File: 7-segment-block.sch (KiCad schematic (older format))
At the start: 23 parts, among them J1 DATA_OUT, J2 DATA_IN, U1 TPIC6C596PWR, U2 74LS125

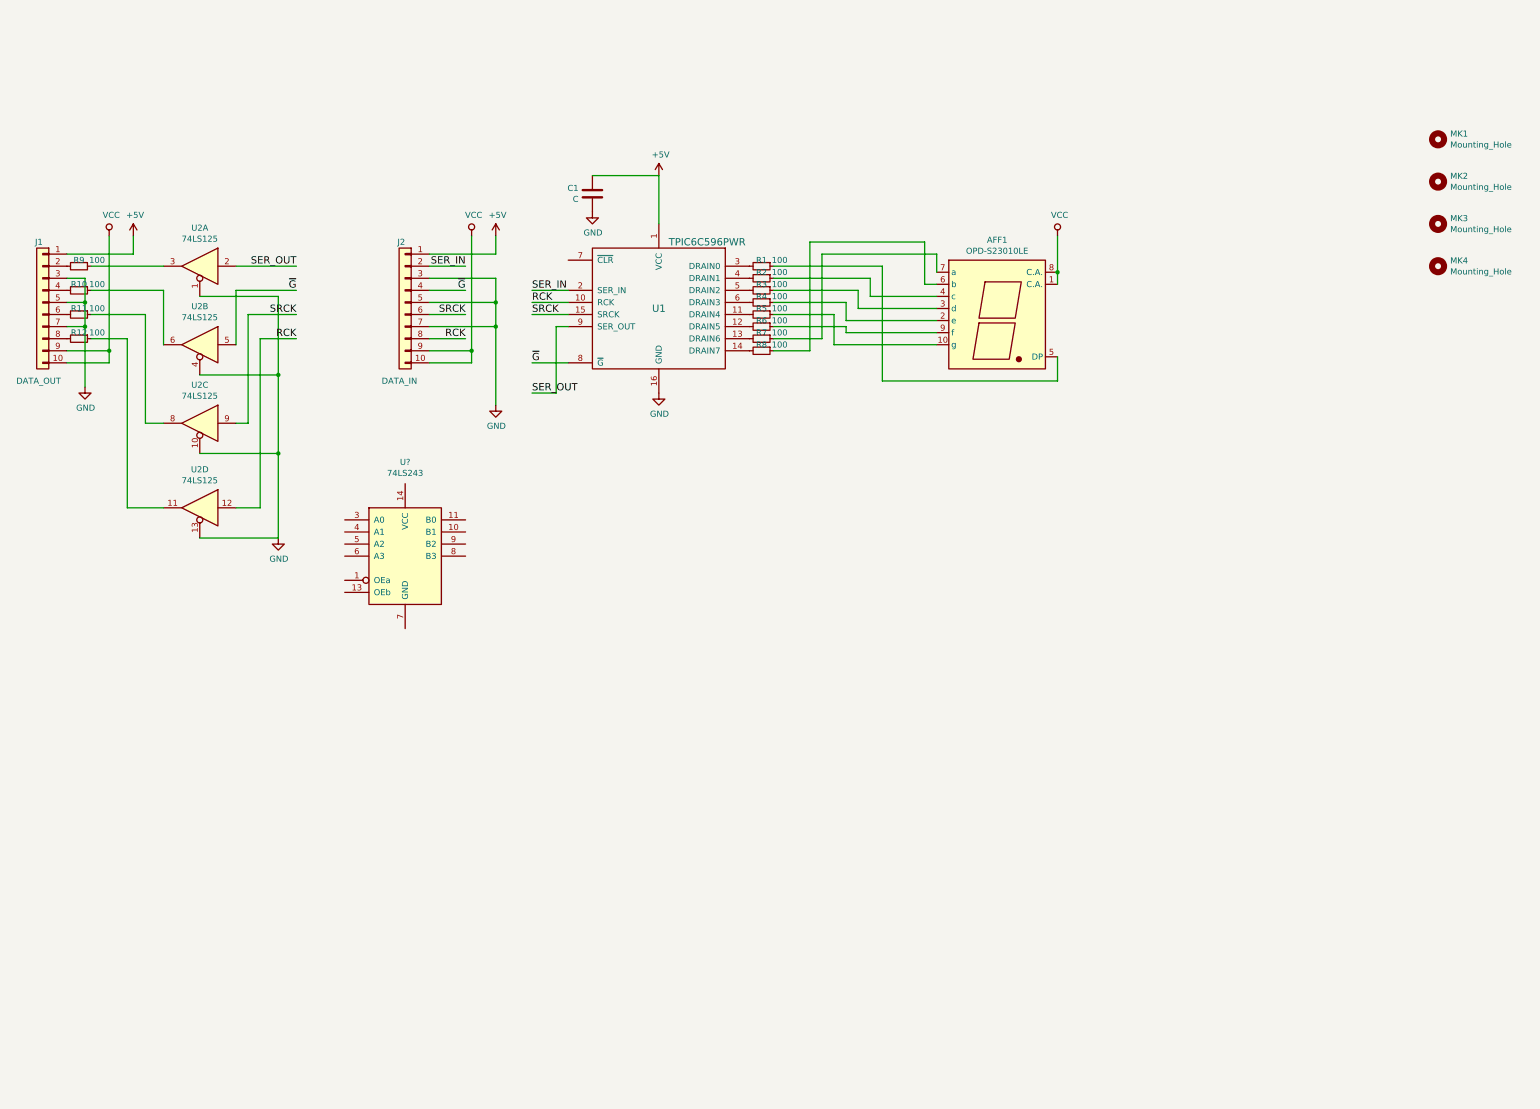
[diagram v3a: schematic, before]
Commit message: Finish routing, change buffer IC, add some decoupling caps
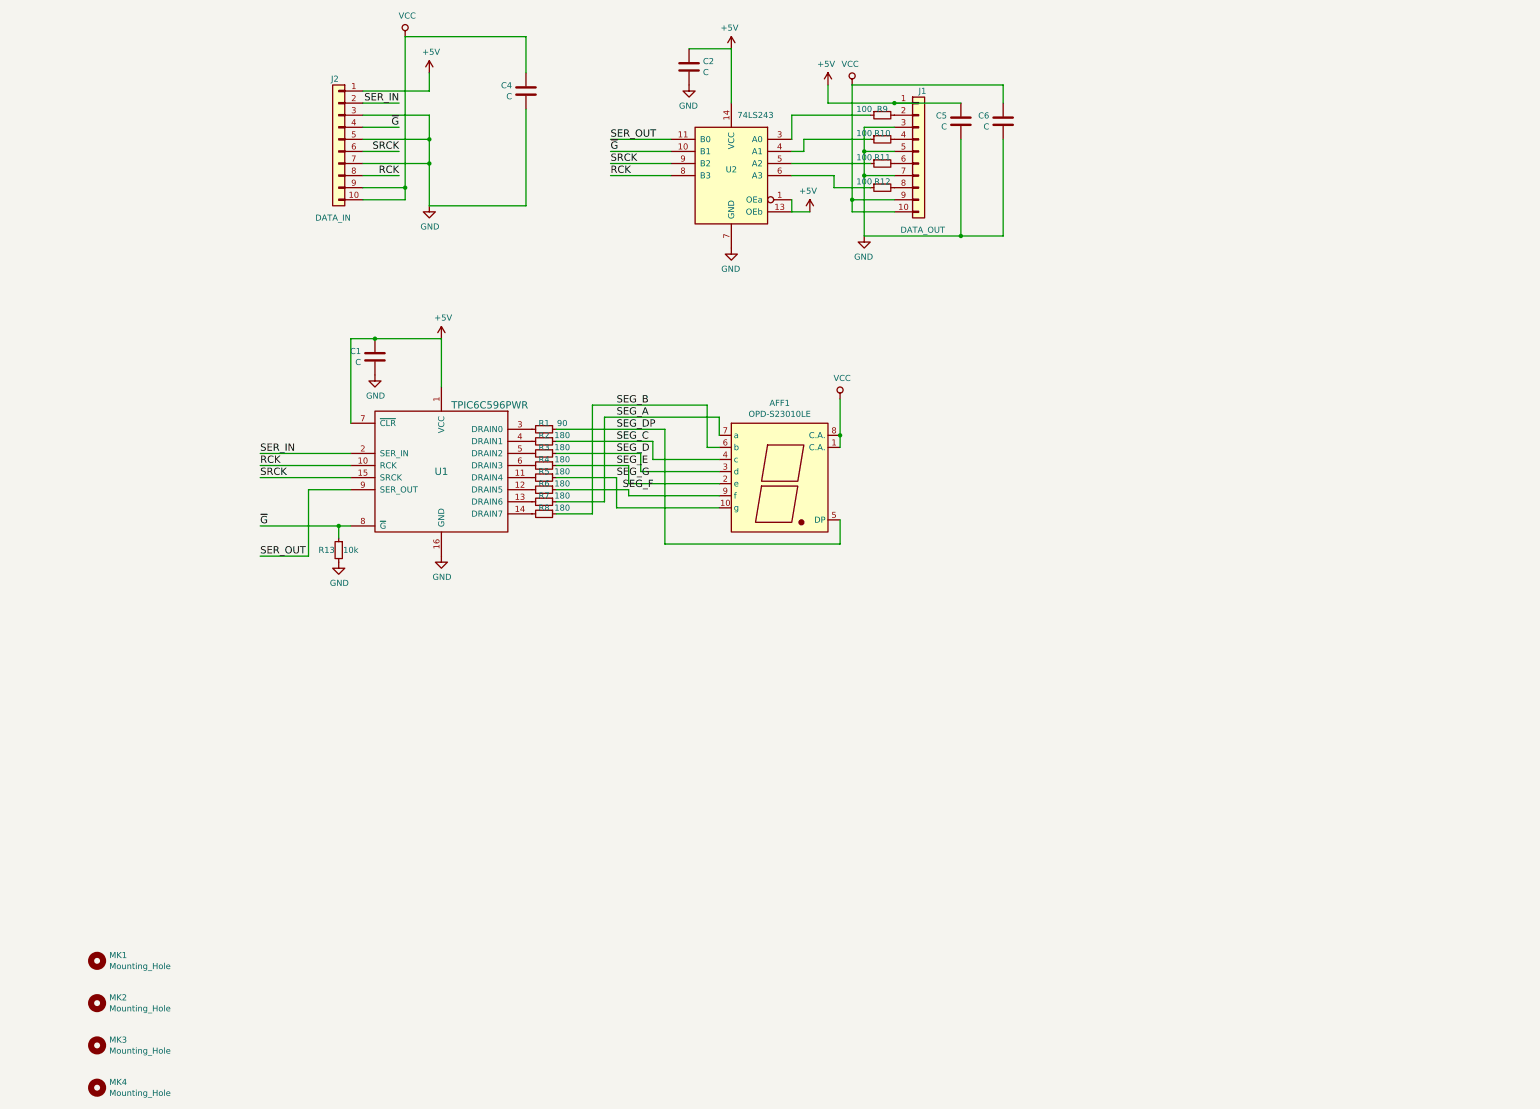
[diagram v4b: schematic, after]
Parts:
- removed U2: 74LS125, Housings_SOIC:SOIC-14_3.9x8.7mm_Pitch1.27mm, symbol Logic_74xx:74LS125
- added C2, C4, C5, C6: C, Capacitors_SMD:C_0805_HandSoldering, symbol device:C
- added R13: 10k, Resistors_SMD:R_0805_HandSoldering, symbol device:R_Small
- R1: value 100 -> 90
- R2, R3, R4, R5, R6, R7, R8: value 100 -> 180
- U2: renamed from U?; footprint (none) -> Housings_SOIC:SOIC-14_3.9x8.7mm_Pitch1.27mm; Distributor (none) -> ?; Manufacturer (none) -> ?; PartNo (none) -> ?
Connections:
- net +5V: now also U1.7 (~CLR), U2.1 (OEa), U2.13 (OEb), U2.14 (VCC), C2.1, C5.1
- net GND: now also U2.7 (GND), C2.2, C4.2, C5.2, C6.2, R13.2
- net RCK: now also U2.8 (B3)
- net SER_OUT: now also U2.11 (B0)
- net SRCK: now also U2.9 (B2)
- net VCC: now also C4.1, C6.1
- net ~G: now also U2.10 (B1), R13.1
- net SEG_G: now reaches AFF1.10 (g), R5.1
- net SEG_E: now reaches AFF1.2 (e), R4.1
- net SEG_D: now reaches AFF1.3 (d), R3.1
- net SEG_C: now reaches AFF1.4 (c), R2.1
- net SEG_DP: now reaches AFF1.5 (DP), R1.1
- net SEG_B: now reaches AFF1.6 (b), R8.1
- net SEG_A: now reaches AFF1.7 (a), R7.1
- net SEG_F: now reaches AFF1.9 (f), R6.1
- net at R9.1: now also U2.3 (A0)
- net at R10.1: now also U2.4 (A1)
- net at R11.1: now also U2.5 (A2)
- net at R12.1: now also U2.6 (A3)
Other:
- moved on the sheet: AFF1, C1, J1, J2, MK1, MK2, MK3, MK4, R1, R10, R11, R12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

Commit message: Add pullup on ~G, send for manufacturing
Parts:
- added R14: 10k, Resistors_SMD:R_0805_HandSoldering, symbol device:R_Small
- C1, C2, C4, C5, C6: value C -> 1u
- R1: value 90 -> 360
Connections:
- net +5V: now also R14.2
- net ~G: now also R14.1
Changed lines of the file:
@@
 P 3450 4250
 F 0 "C1" H 3565 4296 50  0000 L CNN
-F 1 "C" H 3565 4205 50  0000 L CNN
+F 1 "1u" H 3565 4205 50  0000 L CNN
 F 2 "Capacitors_SMD:C_0805_HandSoldering" H 3488 4100 50  0001 C CNN
 F 3 "" H 3450 4250 50  0001 C CNN
@@
 Text Label 2500 5250 0    60   ~ 0
 SRCK
-Text Label 2500 5650 0    60   ~ 0
+Text Label 2200 5650 0    60   ~ 0
 ~G
 $Comp
@@
 P 4850 4850
 F 0 "R1" V 4800 4850 50  0000 C CNN
-F 1 "90" V 4800 5000 50  0000 C CNN
+F 1 "360" V 4800 5000 50  0000 C CNN
 F 2 "Resistors_SMD:R_0805_HandSoldering" H 4850 4850 50  0001 C CNN
 F 3 "" H 4850 4850 50  0001 C CNN
@@
 	6200 5000 6300 5000
 Wire Wire Line
-	3250 4100 4000 4100
+	3250 4100 3450 4100
 Wire Wire Line
 	4000 4100 4000 4500
@@
 	2500 5050 3250 5050
 Wire Wire Line
-	2500 5650 3250 5650
-Wire Wire Line
-	3900 2250 3900 3000
+	2200 5650 2800 5650
+Wire Wire Line
+	3900 2250 3900 2450
 Wire Wire Line
 	3350 2050 3900 2050
@@
 	3900 2050 3900 1900
 Wire Wire Line
-	3700 1600 3700 2950
+	3700 1600 3700 2850
 Wire Wire Line
 	3350 2850 3700 2850
@@
 Connection ~ 3700 2850
 Wire Wire Line
-	3250 5350 2900 5350
-Wire Wire Line
-	2900 5350 2900 5900
-Wire Wire Line
-	2500 5900 2900 5900
-Wire Wire Line
-	7300 4600 7300 5000
+	3250 5350 2600 5350
+Wire Wire Line
+	2600 5350 2600 5900
+Wire Wire Line
+	2200 5900 2600 5900
+Wire Wire Line
+	7300 4600 7300 4900
 Connection ~ 7300 4900
 Wire Wire Line
@@
 $EndComp
 Wire Wire Line
-	7200 2150 8300 2150
+	7200 2150 7750 2150
 Wire Wire Line
 	7200 2150 7200 2000
@@
 $EndComp
 Wire Wire Line
-	7400 2000 7400 3050
+	7400 2000 7400 2950
 Wire Wire Line
 	7750 2950 7400 2950
@@
 	7750 2350 7500 2350
 Wire Wire Line
-	7500 2350 7500 3250
+	7500 2350 7500 2550
 Wire Wire Line
 	7750 2550 7500 2550
@@
 Wire Wire Line
 	7550 2850 7250 2850
-Text Label 2500 5900 0    60   ~ 0
+Text Label 2200 5900 0    60   ~ 0
 SER_OUT
 Wire Wire Line
@@
 P 6050 1850
 F 0 "C2" H 6165 1896 50  0000 L CNN
-F 1 "C" H 6165 1805 50  0000 L CNN
+F 1 "1u" H 6165 1805 50  0000 L CNN
 F 2 "Capacitors_SMD:C_0805_HandSoldering" H 6088 1700 50  0001 C CNN
 F 3 "" H 6050 1850 50  0001 C CNN
@@
 P 8300 2300
 F 0 "C5" H 8415 2346 50  0000 L CNN
-F 1 "C" H 8415 2255 50  0000 L CNN
+F 1 "1u" H 8415 2255 50  0000 L CNN
 F 2 "Capacitors_SMD:C_0805_HandSoldering" H 8338 2150 50  0001 C CNN
 F 3 "" H 8300 2300 50  0001 C CNN
@@
 	8300 2450 8300 3250
 Wire Wire Line
-	7500 3250 8650 3250
+	7500 3250 8300 3250
 $Comp
 L device:C C4
@@
 P 4700 2050
 F 0 "C4" H 4815 2096 50  0000 L CNN
-F 1 "C" H 4815 2005 50  0000 L CNN
+F 1 "1u" H 4815 2005 50  0000 L CNN
 F 2 "Capacitors_SMD:C_0805_HandSoldering" H 4738 1900 50  0001 C CNN
 F 3 "" H 4700 2050 50  0001 C CNN
@@
 P 8650 2300
 F 0 "C6" H 8765 2346 50  0000 L CNN
-F 1 "C" H 8765 2255 50  0000 L CNN
+F 1 "1u" H 8765 2255 50  0000 L CNN
 F 2 "Capacitors_SMD:C_0805_HandSoldering" H 8688 2150 50  0001 C CNN
 F 3 "" H 8650 2300 50  0001 C CNN
@@
 	1    0    0    -1
 $EndComp
+Wire Wire Line
+	3900 2450 3900 2650
+Wire Wire Line
+	3700 2850 3700 2950
+Wire Wire Line
+	7300 4900 7300 5000
+Wire Wire Line
+	3900 2650 3900 3000
+Wire Wire Line
+	7400 2950 7400 3050
+Wire Wire Line
+	7500 2550 7500 2750
+Wire Wire Line
+	7500 2750 7500 3250
+Wire Wire Line
+	7750 2150 8300 2150
+Wire Wire Line
+	8300 3250 8650 3250
+Wire Wire Line
+	3450 4100 4000 4100
+Wire Wire Line
+	3150 5650 3250 5650
+$Comp
+L power:+5V #PWR016
+U 1 1 5A3FC8C4
+P 2800 5950
+F 0 "#PWR016" H 2800 5800 50  0001 C CNN
+F 1 "+5V" H 2815 6123 50  0000 C CNN
+F 2 "" H 2800 5950 50  0001 C CNN
+F 3 "" H 2800 5950 50  0001 C CNN
+	1    2800 5950
+	-1   0    0    1
+$EndComp
+$Comp
+L device:R_Small R14
+U 1 1 5A3FF3B0
+P 2800 5850
+F 0 "R14" H 2900 5850 50  0000 C CNN
+F 1 "10k" H 2700 5850 50  0000 C CNN
+F 2 "Resistors_SMD:R_0805_HandSoldering" H 2800 5850 50  0001 C CNN
+F 3 "" H 2800 5850 50  0001 C CNN
+F 4 "?" H 2800 5850 60  0001 C CNN "PartNo"
+F 5 "?" H 2800 5850 60  0001 C CNN "Manufacturer"
+F 6 "?" H 2800 5850 60  0001 C CNN "Distributor"
+	1    2800 5850
+	-1   0    0    -1
+$EndComp
+Wire Wire Line
+	2800 5750 2800 5650
+Connection ~ 2800 5650
+Wire Wire Line
+	2800 5650 3150 5650
 $EndSCHEMATC

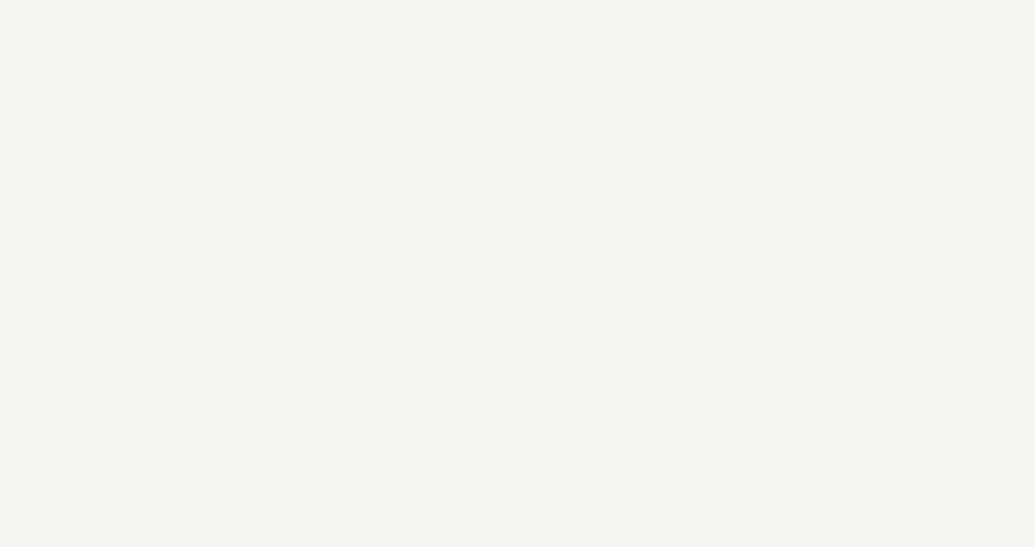
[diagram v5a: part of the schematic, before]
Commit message: Add some lincence notices
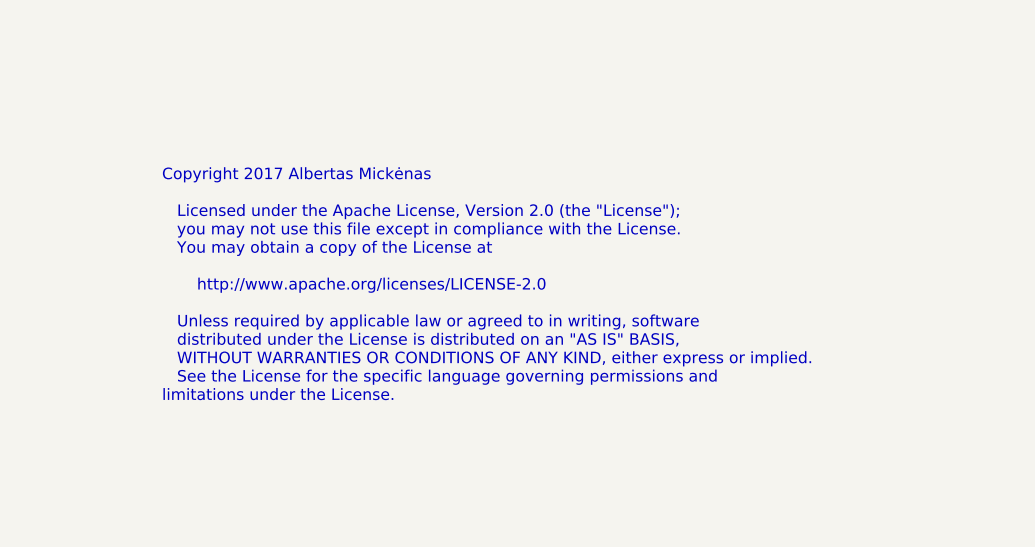
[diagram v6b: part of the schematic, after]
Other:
- note added: "Copyright 2017 Albertas Mickėnas\n\n Licensed under the Apache License, Version 2.0 (the "License");\n you may not use this file except in compliance with the License.\n You may obtain a copy of the License at\n\n http://www.apache.org/licenses/LICENSE-2.0\n\n Unless required by applicable law or agreed to in writing, software\n distributed under the License is distributed on an "AS IS" BASIS,\n 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"
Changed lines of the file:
@@
 Wire Wire Line
 	2800 5650 3150 5650
+Text Notes 11750 9850 0    50   ~ 0
+Copyright 2017 Albertas Mickėnas\n\n   Licensed under the Apache License, Version 2.0 (the "License");\n   you may not use this file except in compliance with the License.\n   You may obtain a copy of the License at\n\n       http://www.apache.org/licenses/LICENSE-2.0\n\n   Unless required by applicable law or agreed to in writing, software\n   distributed under the License is distributed on an "AS IS" BASIS,\n   WITHOUT WARRANTIES OR CONDITIONS OF ANY KIND, either express or implied.\n   See the License for the specific language governing permissions and\nlimitations under the License.
 $EndSCHEMATC
